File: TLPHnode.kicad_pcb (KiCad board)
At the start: 4 copper layers, 28 x 20.5 mm, 30 parts, among them P1 Bat, P2 CONN_01X06, SW1 Reset, U1 NCP703, U2 LD39130S, U3 LPS25HB, U4 Si7006-A20, U5 ESP-12E, U6 ISL29035

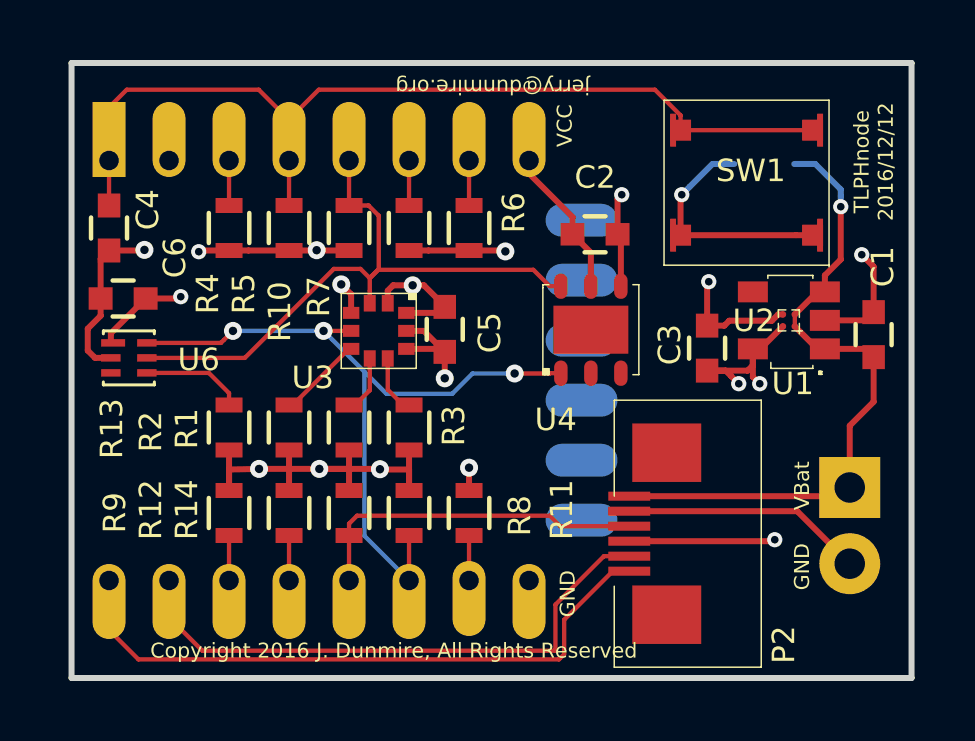
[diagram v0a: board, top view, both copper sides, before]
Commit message: Add Charger control signals to P2
    - All routes removed.

On branch addChrgCtrl
modified:   TLPHnode-cache.lib
modified:   TLPHnode.kicad_pcb
modified:   TLPHnode.net
modified:   TLPHnode.sch
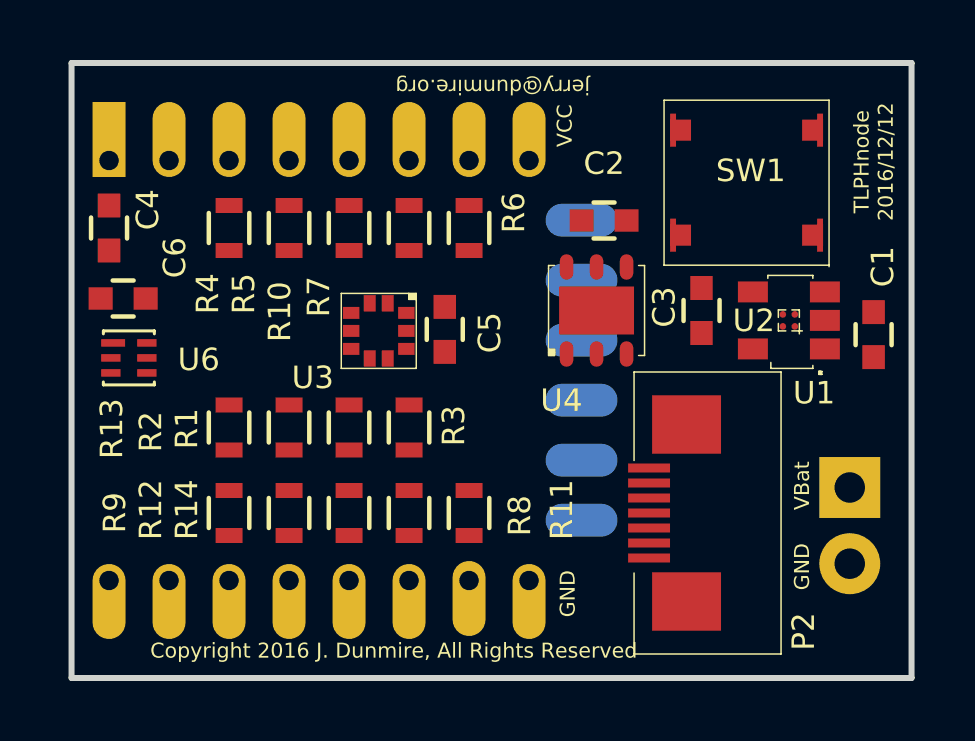
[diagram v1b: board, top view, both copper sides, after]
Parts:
- P2: value CONN_01X06 -> CONN_01X07; footprint rockingdlabs:FPC_conn-6_8x4.9mm_Pitch0.5mm -> rockingdlabs:FPC_conn-7_8x4.9mm_Pitch0.5mm
- R12, R9: value 4.7k -> 10k
- moved C3 1.27 mm to (151.5, 88.8)
- moved P2 0.95 mm to (151.5, 95.5)
- moved U4 0.67 mm to (148.0, 88.8)
- moved C2 0.55 mm to (148.2, 85.8)
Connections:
- P2 pad 3: VCC -> /CTRL
- P2 pad 4: /PGM -> /CHRG
- P2 pad 5: GND -> /PGM
- P2 pad 6: /VBat -> GND
- R12 pad 1: VCC -> /CTRL
- R12 pad 2: Net-(R12-Pad2) -> GND
- R9 pad 2: Net-(R9-Pad2) -> /CHRG
- U5 pad 13: Net-(R12-Pad2) -> /CTRL
- U5 pad 14: Net-(R9-Pad2) -> /CHRG
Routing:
- net VCC: track 45.4 -> 0.00 mm, vias 11 -> 0
- net GND: track 38.2 -> 0.00 mm, vias 8 -> 0
- net Net-(C4-Pad1): track 32.4 -> 0.00 mm
- net /I2C_SDA: track 25.1 -> 0.00 mm, vias 3 -> 0
- net /VBat: track 22.4 -> 0.00 mm, vias 1 -> 0
- net /TXD: track 21.3 -> 0.00 mm
- net /I2C_SCL: track 21.2 -> 0.00 mm
- net /RXD: track 19.2 -> 0.00 mm
- net /PGM: track 11.5 -> 0.00 mm
- net Net-(R13-Pad2): track 3.41 -> 0.00 mm
- net Net-(R2-Pad2): track 2.84 -> 0.00 mm
- net Net-(R3-Pad2): track 1.96 -> 0.00 mm
- net Net-(R1-Pad2): track 1.95 -> 0.00 mm
- net Net-(R9-Pad2): track 1.50 -> 0.00 mm
- net Net-(R7-Pad1): track 1.50 -> 0.00 mm
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
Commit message: Checkpoint - Routing complete, 7-pin P2
    - Includes control and monitoring signals for battery charger

On branch addChrgCtrl
modified:   TLPHnode.kicad_pcb
modified:   TLPHnode.net
modified:   TLPHnode.sch
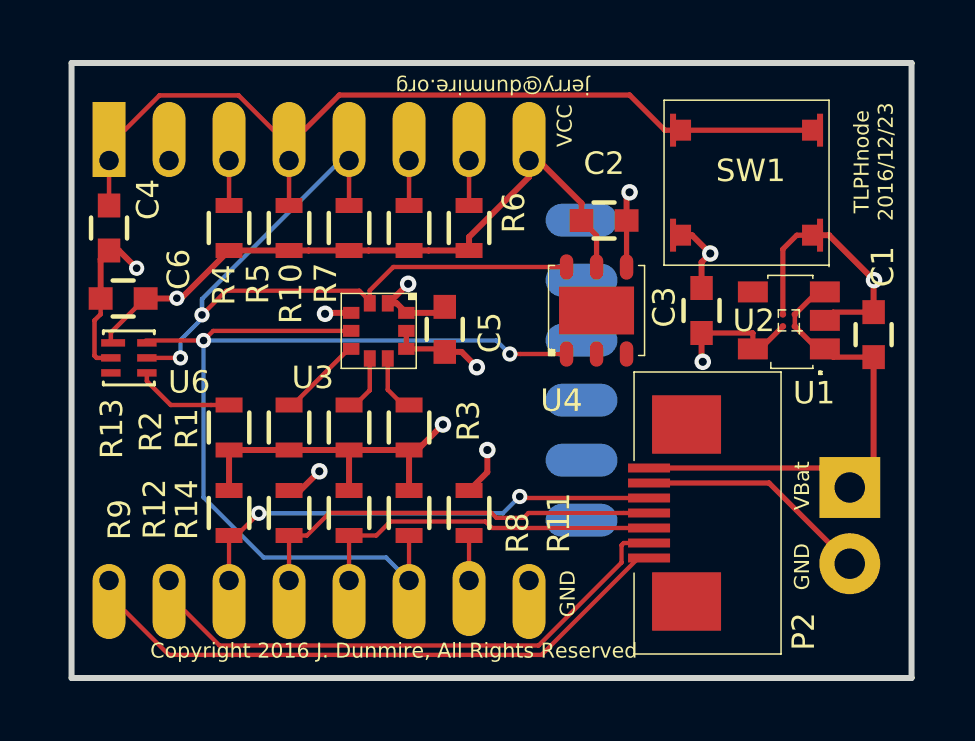
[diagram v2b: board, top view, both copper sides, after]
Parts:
- turned R12 to 90 degrees
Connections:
- P2 pad 3: /CTRL -> /PGM
- P2 pad 4: /CHRG -> /CTRL
- P2 pad 5: /PGM -> /CHRG
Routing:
- net VCC: track 0.00 -> 41.0 mm, vias 0 -> 4
- net GND: track 0.00 -> 34.1 mm, vias 0 -> 8
- net /I2C_SDA: track 0.00 -> 34.0 mm, vias 0 -> 2
- net Net-(C4-Pad1): track 0.00 -> 30.5 mm
- net /I2C_SCL: track 0.00 -> 25.1 mm, vias 0 -> 2
- net /TXD: track 0.00 -> 20.6 mm
- net /RXD: track 0.00 -> 18.9 mm
- net /VBat: track 0.00 -> 16.4 mm
- net /CHRG: track 0.00 -> 16.1 mm, vias 0 -> 2
- net /CTRL: track 0.00 -> 13.9 mm
- net /PGM: track 0.00 -> 11.8 mm
- net Net-(R13-Pad2): track 0.00 -> 3.34 mm
- net Net-(R2-Pad2): track 0.00 -> 2.84 mm
- net Net-(R3-Pad2): track 0.00 -> 1.96 mm
- net Net-(R1-Pad2): track 0.00 -> 1.95 mm
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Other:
- board text added: "TLPHnode 2016/12/23"
- board text removed: "TLPHnode 2016/12/12"
